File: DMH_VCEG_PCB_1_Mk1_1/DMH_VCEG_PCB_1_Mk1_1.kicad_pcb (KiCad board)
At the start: 2 copper layers, 148 x 175 mm, 239 parts, among them J1 TS_Jack_6.35mm_Sw, J10 TS_Jack_6.35mm_Sw, J100 IDC_02x08, J11 TS_Jack_6.35mm_Sw, J12 TS_Jack_6.35mm_Sw, J13 TS_Jack_6.35mm_Sw, J14 TS_Jack_6.35mm_Sw, J15 TS_Jack_6.35mm_Sw, J16 TS_Jack_6.35mm_Sw, J17 TS_Jack_6.35mm_Sw, J18 TS_Jack_6.35mm_Sw, J19 TS_Jack_6.35mm_Sw, J2 TS_Jack_6.35mm_Sw, J20 TS_Jack_6.35mm_Sw, J200 IDC_02x08, J21 Conn_01x10_PinHeader, J22 Conn_01x10_PinHeader, J23 Conn_01x10_PinHeader, J24 Conn_01x06_PinHeader, J25 Conn_01x10_PinHeader, J26 Conn_01x10_PinHeader, J27 Conn_01x10_PinHeader, J3 TS_Jack_6.35mm_Sw, J4 TS_Jack_6.35mm_Sw, J5 TS_Jack_6.35mm_Sw, J6 TS_Jack_6.35mm_Sw, J7 TS_Jack_6.35mm_Sw, J8 TS_Jack_6.35mm_Sw, J9 TS_Jack_6.35mm_Sw, Q1 BC558, Q17 BC558, Q18 BC558, Q19 BC548, Q2 BC558, Q20 BC548, Q21 BS170, Q22 BS170, Q3 BC548, Q4 BC548, Q5 BS170, Q6 BS170, U1 TL074, U11 TL074, U12 4001, U13 40106, U15 TL074, U16 4001, U17 TL074, U2 4001, U25 4001, U3 40106, U5 TL074, U6 4001, U7 TL074

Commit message: Redesigned PCB 1
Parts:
- removed Q21, Q22: BS170, Package_TO_SOT_THT:TO-92_Inline
- removed R100: 100k, Resistor_THT:R_Axial_DIN0207_L6.3mm_D2.5mm_P7.62mm_Horizontal
- removed R103, R6: 82k, Resistor_THT:R_Axial_DIN0207_L6.3mm_D2.5mm_P7.62mm_Horizontal
- removed RV2, RV23: 50k, Potentiometer_THT:Potentiometer_Bourns_3296W_Vertical
- added C79: 100nF, Capacitor_THT:C_Disc_D4.3mm_W1.9mm_P5.00mm, B.Cu at (97.5, 92.8)
- added R202: 100k, Resistor_THT:R_Axial_DIN0207_L6.3mm_D2.5mm_P7.62mm_Horizontal, B.Cu at (40.1, 77.8)
- added U26: CD4066BE, Package_DIP:DIP-14_W7.62mm_Socket, B.Cu at (103.8, 95.6)
- Q5, Q6: value BS170 -> BC548; footprint Package_TO_SOT_THT:TO-92_Inline -> Package_TO_SOT_THT:TO-92L_Inline_Wide
- R105, R8: value 100k -> 150k
- moved R3 97.6 mm to (159.9, 77.9)
- moved Q6 77.6 mm to (151.3, 85.5)
- moved Q5 45.9 mm to (48.7, 85.5), turned to 180 degrees
- moved D25 0.30 mm to (135.0, 71.5)
- moved D26 0.30 mm to (140.0, 71.5)
- moved D6 0.30 mm to (65.0, 71.5)
- moved D7 0.30 mm to (60.0, 71.5)
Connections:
- J1 pad T: Net-(J22B-Pin_2) -> /Inputs and Outputs A/Att CV A T
- J11 pad TN: /CV Processing A/Att CV -> /Inputs and Outputs A/Att CV A T
- J12 pad TN: /CV Processing A/Dec CV -> /Inputs and Outputs A/Dec CV A T
- J13 pad TN: /CV Processing A/Sus CV -> /Inputs and Outputs A/Sus CV A T
- J14 pad TN: /CV Processing A/Rel CV -> /Inputs and Outputs A/Rel CV A T
- J15 pad TN: /Core Circuit A/Gate -> /Inputs and Outputs A/Gate A TN
- J2 pad T: Net-(J22D-Pin_4) -> /Inputs and Outputs A/Dec CV A T
- J22 pad 2: Net-(J22B-Pin_2) -> /Inputs and Outputs A/Att CV A T
- J22 pad 4: Net-(J22D-Pin_4) -> /Inputs and Outputs A/Dec CV A T
- J23 pad 3: Net-(J23C-Pin_3) -> /Inputs and Outputs A/Sus CV A T
- J23 pad 8: Net-(J23H-Pin_8) -> /Inputs and Outputs A/Rel CV A T
- J3 pad T: Net-(J23C-Pin_3) -> /Inputs and Outputs A/Sus CV A T
- J4 pad T: Net-(J23H-Pin_8) -> /Inputs and Outputs A/Rel CV A T
- Q5 pad 1: Net-(J23J-Pin_10) -> +12V
- Q5 pad 2: /Core Circuit A/ProcGate -> /CV Processing A/Max Level
- Q5 pad 3: Net-(Q2-C) -> Net-(Q2-E)
- Q6 pad 1: Net-(J23J-Pin_10) -> +12V
- Q6 pad 2: /Core Circuit A/InvGate -> /CV Processing B/Max Level
- Q6 pad 3: Net-(Q4-C) -> Net-(Q18-E)
- R3 pad 1: /Core Circuit A/InvGate -> GND
- R3 pad 2: Net-(U7D--) -> Net-(Q18-E)
- RV1 pad 1: Net-(U7D--) -> GND
- RV1 pad 2: Net-(Q2-E) -> Net-(U7C-+)
- RV1 pad 3: Net-(Q2-E) -> Net-(U7D--)
- RV22 pad 1: Net-(U17A--) -> GND
- RV22 pad 2: Net-(Q18-E) -> Net-(U17B-+)
- RV22 pad 3: Net-(Q18-E) -> Net-(U17A--)
- U17 pad 1: Net-(Q18-E) -> Net-(U17A--)
- U17 pad 3: GND -> Net-(J27J-Pin_10)
- U17 pad 5: Net-(J27J-Pin_10) -> Net-(U17B-+)
- U7 pad 10: Net-(J23J-Pin_10) -> Net-(U7C-+)
- U7 pad 12: GND -> Net-(J23J-Pin_10)
- U7 pad 14: Net-(Q2-E) -> Net-(U7D--)
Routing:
- net /Inputs and Outputs A/Att CV A T: track 0.00 -> 301.8 mm
- net /CV Processing A/Att CV: track 265.2 -> 0.00 mm, vias 1 -> 0
- net /CV Processing A/Dec CV: track 258.9 -> 0.00 mm, vias 2 -> 0
- net /CV Processing A/Sus CV: track 242.3 -> 0.00 mm, vias 1 -> 0
- net /Inputs and Outputs A/Sus CV A T: track 0.00 -> 242.0 mm
- net /Inputs and Outputs A/Dec CV A T: track 0.00 -> 226.4 mm, vias 0 -> 1
- net /CV Processing A/Rel CV: track 168.7 -> 0.00 mm, vias 1 -> 0
- net Net-(J23C-Pin_3): track 149.6 -> 0.00 mm
- net /Inputs and Outputs A/Rel CV A T: track 0.00 -> 130.8 mm, vias 0 -> 1
- net Net-(J22B-Pin_2): track 107.4 -> 0.00 mm
- net Net-(J22D-Pin_4): track 103.3 -> 0.00 mm
- net Net-(U7D--): track 113.4 -> 17.7 mm, vias 1 -> 0
- net Net-(J23H-Pin_8): track 95.0 -> 0.00 mm, vias 1 -> 0
- net Net-(U17A--): track 82.2 -> 11.4 mm, vias 1 -> 0
- net +12V: track 575.5 -> 627.5 mm
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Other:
- board text added: "Mk1.1 - December 2025"
- board text removed: "Mk1.0 - October 2025"

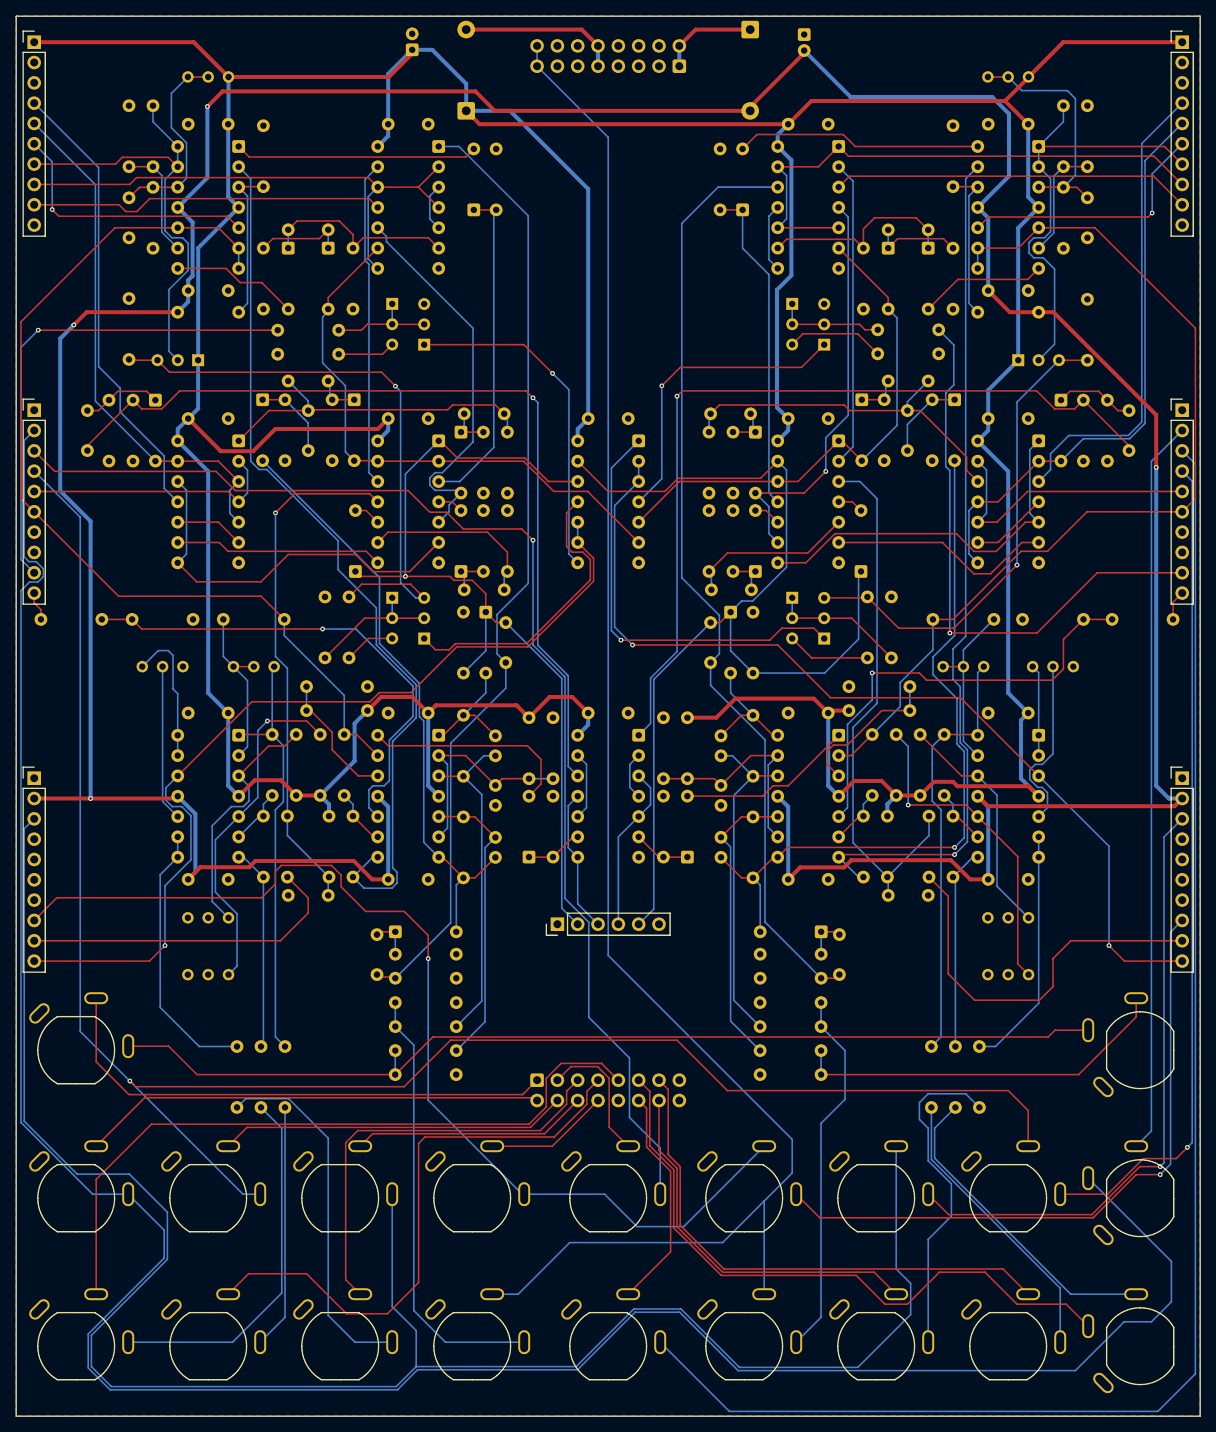
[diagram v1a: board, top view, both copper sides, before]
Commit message: Added diodes to Sustain Gate outputs
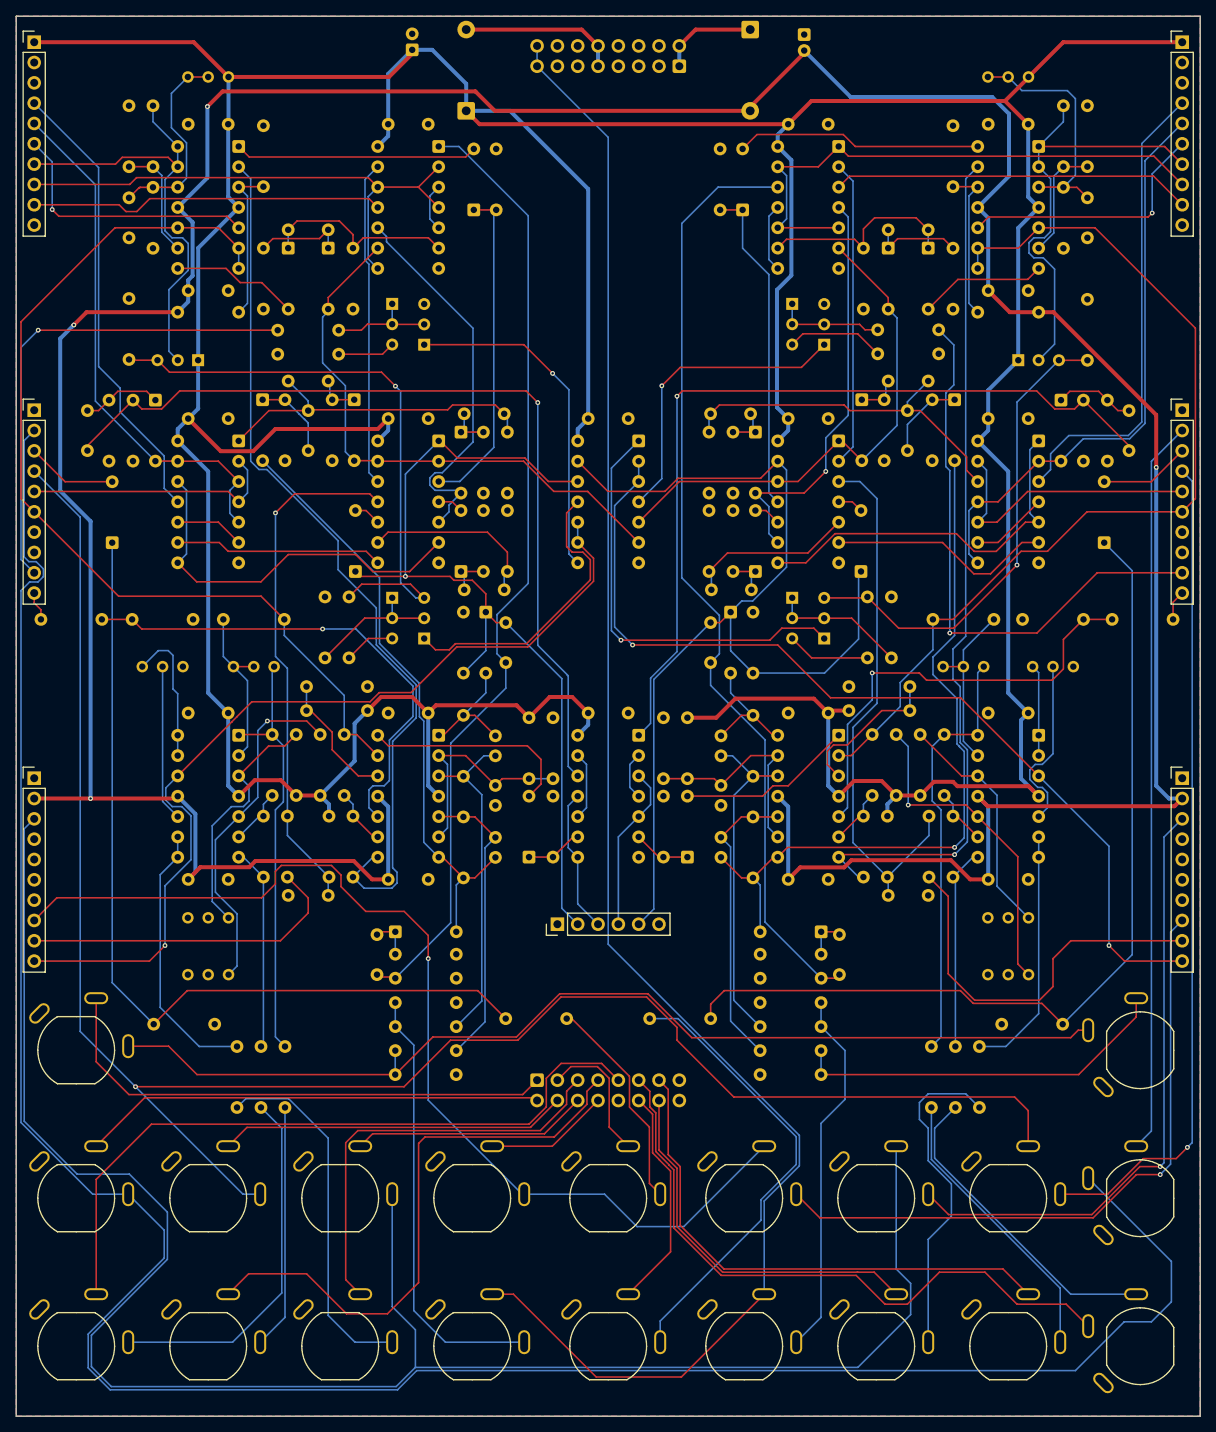
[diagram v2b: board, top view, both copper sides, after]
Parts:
- added D45: 1N4148, Diode_THT:D_DO-35_SOD27_P7.62mm_Horizontal, B.Cu at (38.0, 108.3)
- added D46: 1N4148, Diode_THT:D_DO-35_SOD27_P7.62mm_Horizontal, B.Cu at (162.0, 108.3)
- added R100: 100k, Resistor_THT:R_Axial_DIN0207_L6.3mm_D2.5mm_P7.62mm_Horizontal, B.Cu at (43.2, 168.5)
- added R103: 1k, Resistor_THT:R_Axial_DIN0207_L6.3mm_D2.5mm_P7.62mm_Horizontal, B.Cu at (105.2, 167.8)
- added R200: 100k, Resistor_THT:R_Axial_DIN0207_L6.3mm_D2.5mm_P7.62mm_Horizontal, B.Cu at (156.8, 168.5)
- added R6: 1k, Resistor_THT:R_Axial_DIN0207_L6.3mm_D2.5mm_P7.62mm_Horizontal, B.Cu at (94.8, 167.8)
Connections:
- J17 pad T: Net-(J26C-Pin_3) -> Net-(J17-PadT)
- J22 pad 3: Net-(J22C-Pin_3) -> Net-(D45-A)
- J26 pad 3: Net-(J26C-Pin_3) -> Net-(D46-A)
- J7 pad T: Net-(J22C-Pin_3) -> Net-(J7-PadT)
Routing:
- net Net-(J26C-Pin_3): track 188.5 -> 0.00 mm
- net Net-(J22C-Pin_3): track 155.3 -> 0.00 mm, vias 1 -> 0
- net Net-(D46-K): track 0.00 -> 113.5 mm
- net Net-(D45-K): track 0.00 -> 109.5 mm
- net Net-(J17-PadT): track 0.00 -> 57.2 mm
- net Net-(J7-PadT): track 0.00 -> 27.2 mm
- net Net-(D45-A): track 0.00 -> 11.3 mm
- net Net-(D46-A): track 0.00 -> 11.3 mm
- net /Inputs and Outputs A/Att CV A T: track 301.8 -> 295.8 mm
- net /Inputs and Outputs A/Sus CV A T: track 242.0 -> 236.0 mm
- net /Core Circuit A/Trig: track 126.8 -> 131.3 mm
- net /Inputs and Outputs A/Gate A TN: track 209.5 -> 214.0 mm
- net /Inputs and Outputs A/Dec CV A T: track 226.4 -> 230.8 mm
- net Net-(U17B--): track 30.5 -> 31.2 mm
